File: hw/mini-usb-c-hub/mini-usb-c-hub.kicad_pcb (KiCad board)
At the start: 4 copper layers, 56 x 30 mm, 46 parts, among them J101 USB_C_Receptacle_USB2.0_16P, J201 USB_C_Receptacle_USB2.0_16P, J301 USB_C_Receptacle_USB2.0_16P, J401 USB_A, J501 USB_A, U101 FE1.1s, Y101 12MHz

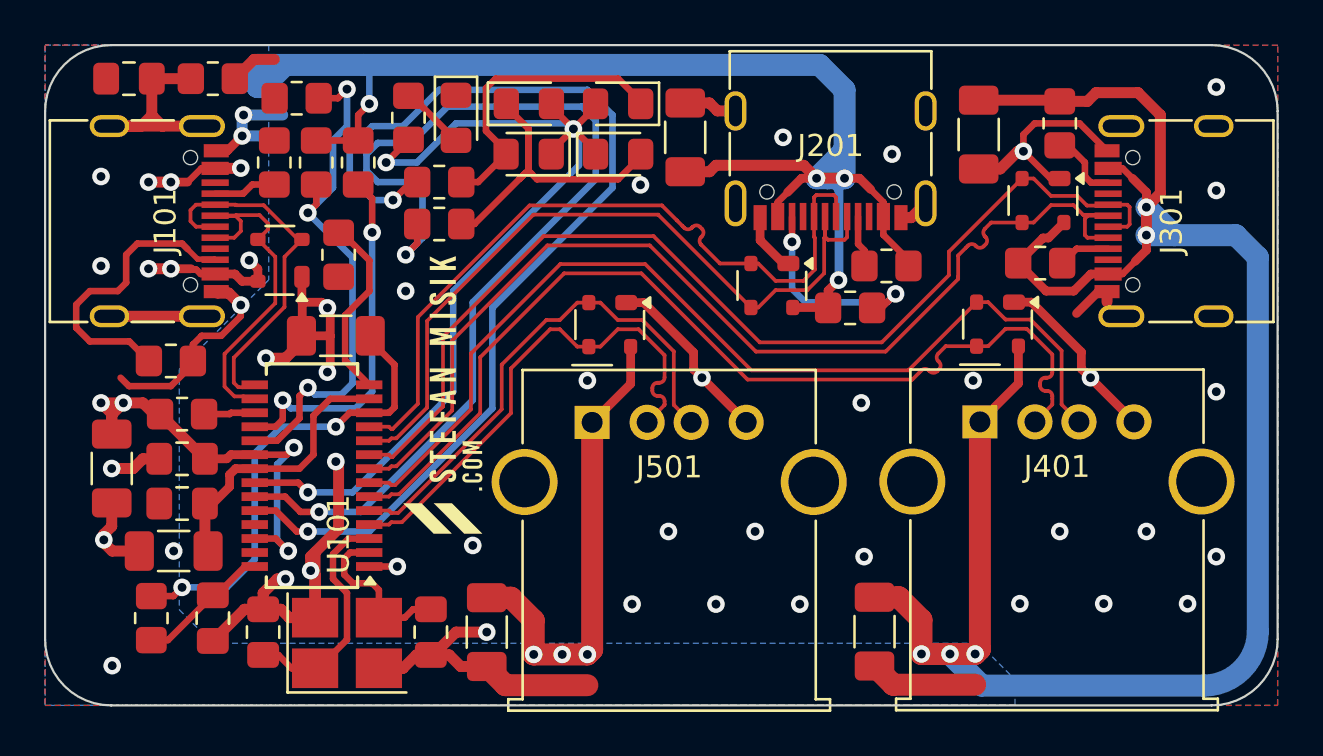
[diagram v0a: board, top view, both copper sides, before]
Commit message: Minor layout improvements
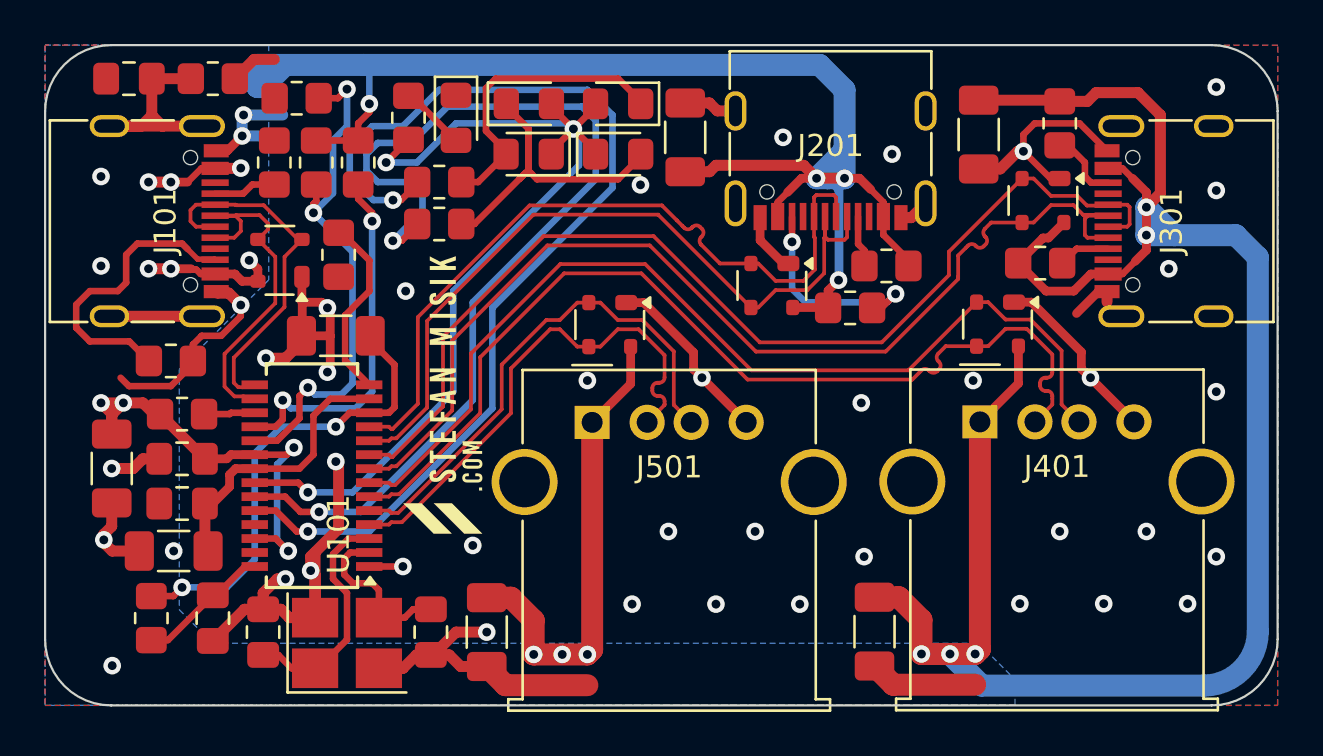
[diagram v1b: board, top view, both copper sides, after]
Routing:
- net /LED1: track 47.3 -> 46.7 mm
- net GND: track 107.0 -> 107.2 mm, vias 43 -> 44
